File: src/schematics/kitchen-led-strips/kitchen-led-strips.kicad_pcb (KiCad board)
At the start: 4 copper layers, 55.5 x 80 mm, 73 parts, among them Q1 BC847BS, Q2 BC847BS, U1 DML3006LFDS, U2 AP62150WU, U3 PIC16F15355-I/MV

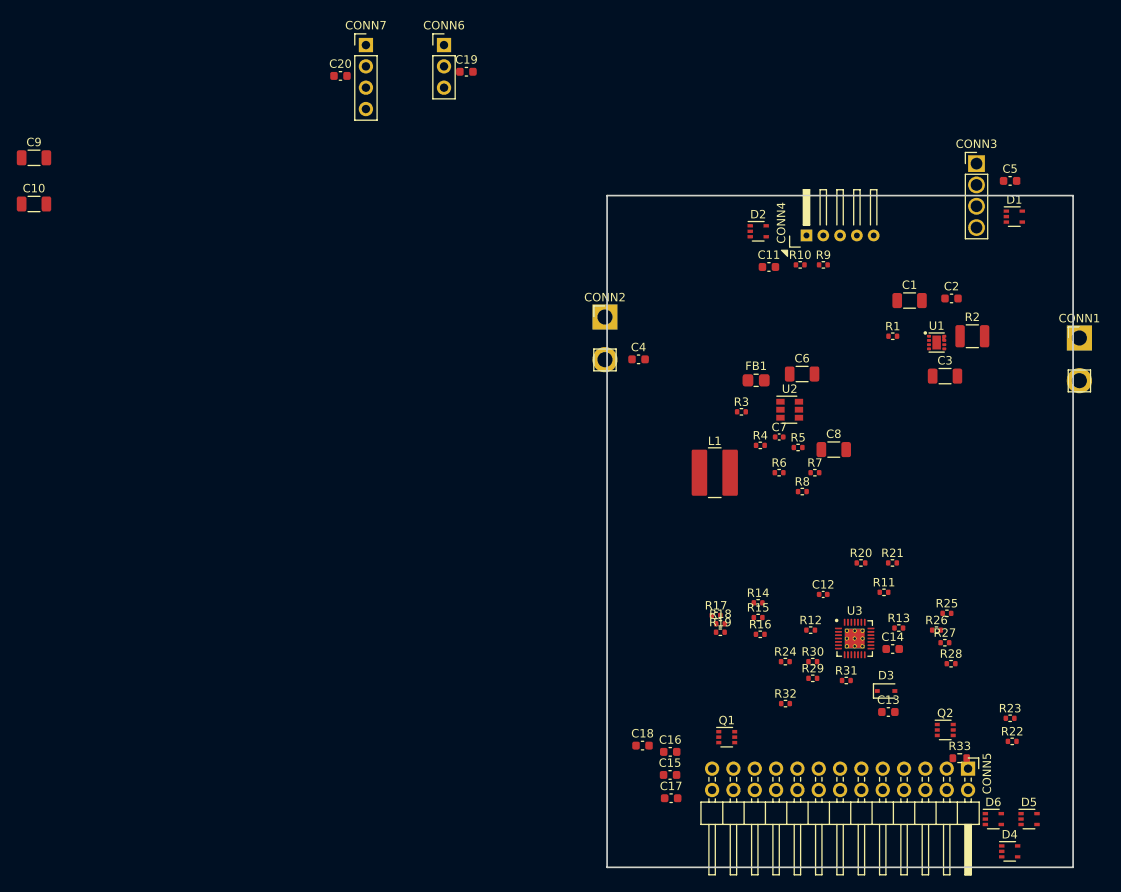
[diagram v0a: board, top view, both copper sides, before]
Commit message: Started the PCB layout.
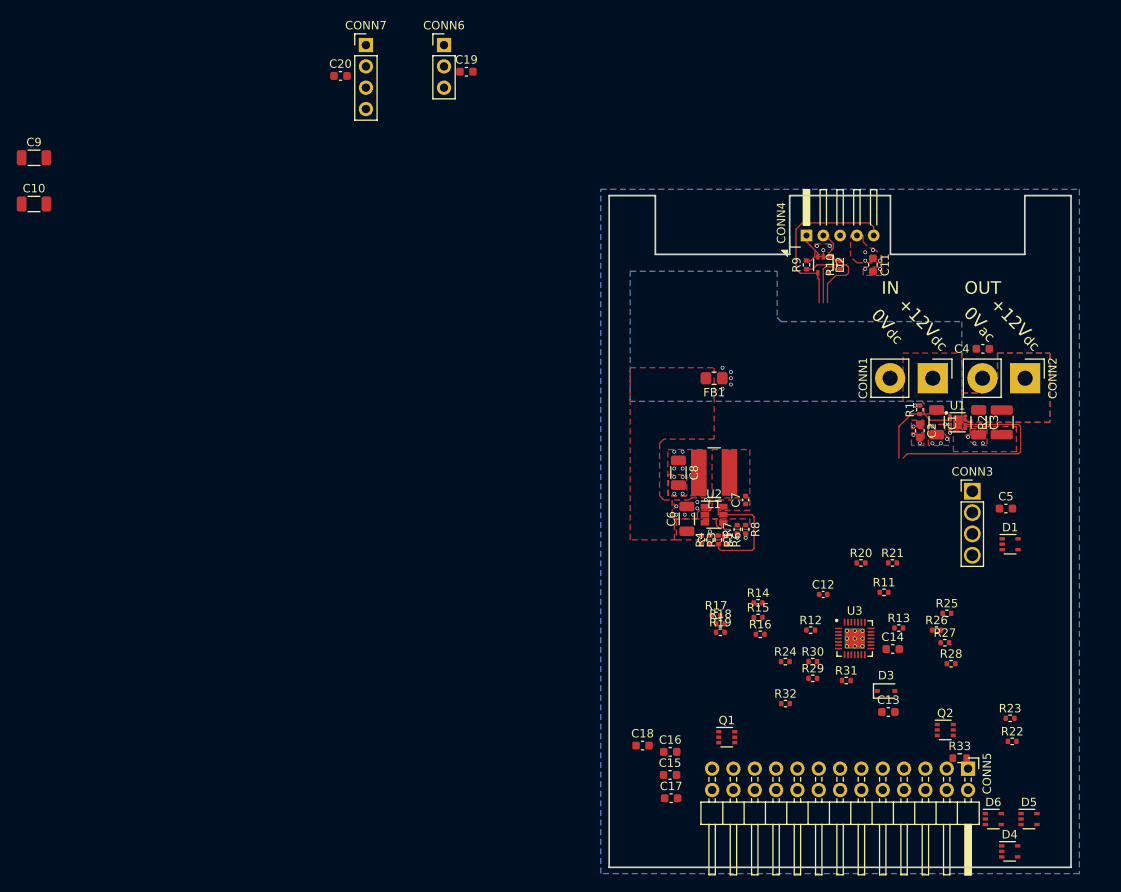
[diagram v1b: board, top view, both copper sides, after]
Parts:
- CONN1, CONN2: footprint restall-generic-connectors:th-header-1x2-5.08mm-vertical -> kitchen-led-strips:th-pads-1x2-5.08mm-vertical-2.5mm^2-solder-pads
- moved CONN2 47.7 mm to (219.5, 121.8), turned to -90 degrees
- moved C4 41.0 mm to (217.0, 118.2)
- moved C5 39.0 mm to (219.8, 137.3)
- moved CONN3 39.0 mm to (215.8, 139.0)
- moved D1 39.0 mm to (220.2, 141.5)
- moved C6 22.0 mm to (181.8, 138.5), turned to 90 degrees
- moved CONN1 20.1 mm to (208.5, 121.8), turned to -90 degrees
- moved C8 18.7 mm to (180.8, 133.0), turned to -90 degrees
- moved C2 16.2 mm to (209.5, 128.0), turned to -90 degrees
- moved R3 16.0 mm to (183.5, 141.0), turned to -90 degrees
- moved U2 15.4 mm to (185.0, 138.0)
- moved C1 14.9 mm to (211.5, 127.0), turned to -90 degrees
- moved R5 14.5 mm to (185.5, 141.0), turned to -90 degrees
- moved R4 12.8 mm to (184.5, 141.0), turned to 90 degrees
- moved C11 12.4 mm to (203.9, 108.2), turned to -90 degrees
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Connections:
- D2 pad 1: /MCU_ICSP_{CLK} -> /MCU_ICSP_{DAT}
- D2 pad 3: /MCU_ICSP_{DAT} -> /MCU_ICSP_{CLK}
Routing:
- net /VLED_{PG}: track 0.00 -> 24.0 mm
- net /~{MCU_MCLR}: track 0.00 -> 22.0 mm
- net Net-(R5-Pad2): track 0.00 -> 13.9 mm
- net Net-(R9-Pad1): track 0.00 -> 11.3 mm
- net /VLED_{EN}: track 0.00 -> 10.8 mm
- net Net-(R10-Pad1): track 0.00 -> 6.21 mm
- net /MCU_ICSP_{DAT}: track 0.00 -> 4.97 mm
- net /MCU_ICSP_{CLK}: track 0.00 -> 4.64 mm
- net GND: track 0.00 -> 3.39 mm, vias 0 -> 30
- net +5Vdc: track 0.00 -> 1.15 mm, vias 0 -> 15
- net /VLED: track 0.00 -> 1.03 mm
- net +12V_{dc}: vias 0 -> 1
- added copper zone on B.Cu, net +12V_{dc}
- added copper zone on F.Cu, net +12V_{dc}
- added copper zone on B.Cu, net +5Vdc
- added copper zone on F.Cu, net +5Vdc
- added copper zone on B.Cu, net /VLED
- added copper zone on F.Cu, net /VLED
- added copper zone on F.Cu, net GND
- added copper zone on In1.Cu, net GND
- added copper zone on In2.Cu, net GND
- added copper zone on F.Cu, net Net-(C1-Pad1)
- added copper zone on F.Cu, net Net-(C7-Pad1)
- added copper zone on F.Cu, net Net-(C7-Pad2)
- added copper zone on F.Cu, net Net-(R2-Pad1)
- added copper zone on F.Cu, net Net-(R7-Pad2)
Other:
- board size 55.5 x 80 mm -> 55 x 80 mm
- board text added: "+12V_{dc}"
- board text added: "0V_{ac}"
- board text added: "0V_{dc}"
- board text added: "IN"
- board text added: "OUT"
- board text added: "TODO: MIGHT BE NECESSARY TO MOVE +12V_{dc} ZONE FROM BOTTOM CU TO TOP CU SOONER, SO THAT +5V_{dc} CAN RUN ON BOTTOM CU UP THE LEFT-HAND-SIDE TO GET TO ICSP HEADER"
- board text added: "TODO: PLACE CONN3 NICELY"
- board text added: "TODO: PLACE SMPS NICELY"
- board text removed: "TODO: SHAPE / CUT BOARD OUTLINE FOR CONNECTOR NUTS"
- board text removed: "TODO: VIA PADS ONLY ON LAYERS THAT CONNECT; FOR THROUGH-HOLE PINS IT'S TOP, BOTTOM AND LAYERS THAT CONNECT"

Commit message: Further elaboration of the PCB.
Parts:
- moved C5 38.4 mm to (186.0, 119.0), turned to 180 degrees
- moved D1 37.9 mm to (186.0, 125.2), turned to -90 degrees
- moved D5 34.8 mm to (184.8, 164.8), turned to 90 degrees
- moved CONN3 34.4 mm to (186.0, 121.8), turned to -90 degrees
- moved C17 28.6 mm to (207.8, 165.5), turned to 180 degrees
- moved R33 26.2 mm to (188.5, 162.0)
- moved Q1 25.0 mm to (211.5, 164.8)
- moved D4 24.4 mm to (200.0, 164.8), turned to 90 degrees
- moved Q2 24.1 mm to (188.5, 164.8)
- moved C16 24.0 mm to (203.8, 165.5)
- moved R28 16.2 mm to (197.2, 158.8), turned to 90 degrees
- moved R25 16.0 mm to (200.2, 159.8), turned to 90 degrees
- moved R27 15.3 mm to (198.2, 158.8), turned to 90 degrees
- moved D6 14.2 mm to (215.2, 164.8), turned to 90 degrees
- moved R26 14.1 mm to (199.2, 158.8), turned to 90 degrees
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- renumbered D5 to D4, D6 to D5, D4 to D6
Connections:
- CONN5 pad 1: /IR_REC -> /I^{2}C_SDA
- CONN5 pad 13: /GPOC_{1} -> /GPIO_{3}
- CONN5 pad 15: /GPOC_{0} -> /GPIO_{2}
- CONN5 pad 17: +5Vdc -> /GPIO_{1}
- CONN5 pad 19: /GPIO_{3} -> /GPIO_{0}
- CONN5 pad 2: +5Vdc -> GND
- CONN5 pad 21: /GPIO_{2} -> +5Vdc
- CONN5 pad 23: /GPIO_{1} -> /IR_LED
- CONN5 pad 25: /GPIO_{0} -> /IR_REC
- CONN5 pad 26: GND -> +5Vdc
- CONN5 pad 3: /IR_LED -> /I^{2}C_SCL
- CONN5 pad 7: /I^{2}C_SDA -> /GPOC_{1}
- CONN5 pad 9: /I^{2}C_SCL -> /GPOC_{0}
- D1 pad 1: /LED_{D1} -> +5Vdc
- D1 pad 3: /LED_{D0} -> +5Vdc
- D1 pad 4: +5Vdc -> /LED_{D1}
- D1 pad 5: +5Vdc -> /LED_{D0}
- D4 pad 4: /GPIO_{2} -> /GPIO_{3}
- D4 pad 5: /GPIO_{3} -> /GPIO_{2}
- D5 pad 1: /GPOC_{1} -> /IR_LED
- D5 pad 3: /GPOC_{0} -> /IR_REC
- D6 pad 1: /IR_LED -> /GPOC_{1}
- D6 pad 3: /IR_REC -> /I^{2}C_SCL
- D6 pad 4: /I^{2}C_SCL -> /I^{2}C_SDA
- D6 pad 5: /I^{2}C_SDA -> /GPOC_{0}
- Q1 pad 3: /GPOC_{1} -> /GPOC_{0}
- Q1 pad 6: /GPOC_{0} -> /GPOC_{1}
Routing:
- net Net-(R9-Pad1): track 11.3 -> 53.8 mm
- net Net-(R10-Pad1): track 6.21 -> 48.0 mm
- net /~{MCU_MCLR}: track 22.0 -> 63.2 mm
- net /LED_{D1}: track 0.00 -> 40.0 mm
- net /LED_{D0}: track 0.00 -> 39.3 mm
- net /VLED_{PG}: track 24.0 -> 58.8 mm
- net /VLED_{EN}: track 10.8 -> 37.7 mm
- net /I^{2}C_SDA: track 0.00 -> 23.5 mm
- net /I^{2}C_SCL: track 0.00 -> 22.7 mm
- net /GPOC_{0}: track 0.00 -> 18.2 mm
- net /GPOC_{1}: track 0.00 -> 14.1 mm
- net Net-(Q1-Pad5): track 0.00 -> 12.9 mm
- net Net-(Q1-Pad2): track 0.00 -> 11.7 mm
- net /VIN_{MON}: track 0.00 -> 7.67 mm
- net /DEBUG_{0}: track 0.00 -> 7.31 mm
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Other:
- board text added: "TODO: PLACE SMPS NICELY - MAYBE OVER THE RHS OF THE BOARD ?"
- board text added: "TODO: THIS CONNECTOR IS 'IN' (LHS WHEN LOOKING AT CASE)"
- board text added: "TODO: THIS CONNECTOR IS 'OUT' (RHS WHEN LOOKING AT CASE)"
- board text removed: "TODO: MIGHT BE NECESSARY TO MOVE +12V_{dc} ZONE FROM BOTTOM CU TO TOP CU SOONER, SO THAT +5V_{dc} CAN RUN ON BOTTOM CU UP THE LEFT-HAND-SIDE TO GET TO ICSP HEADER"
- board text removed: "TODO: PLACE CONN3 NICELY"
- board text removed: "TODO: PLACE SMPS NICELY"

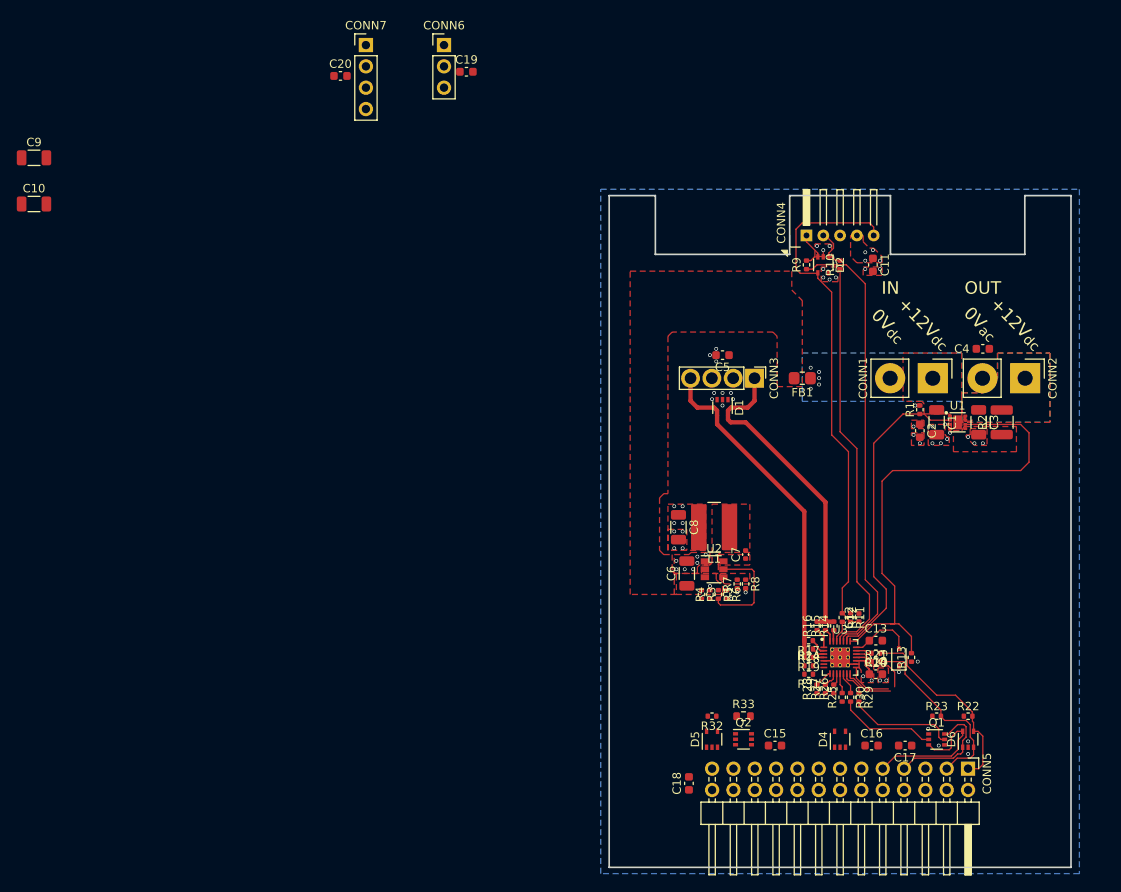
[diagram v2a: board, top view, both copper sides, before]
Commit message: Further PCB elaboration.  Almost ready for fabrication.
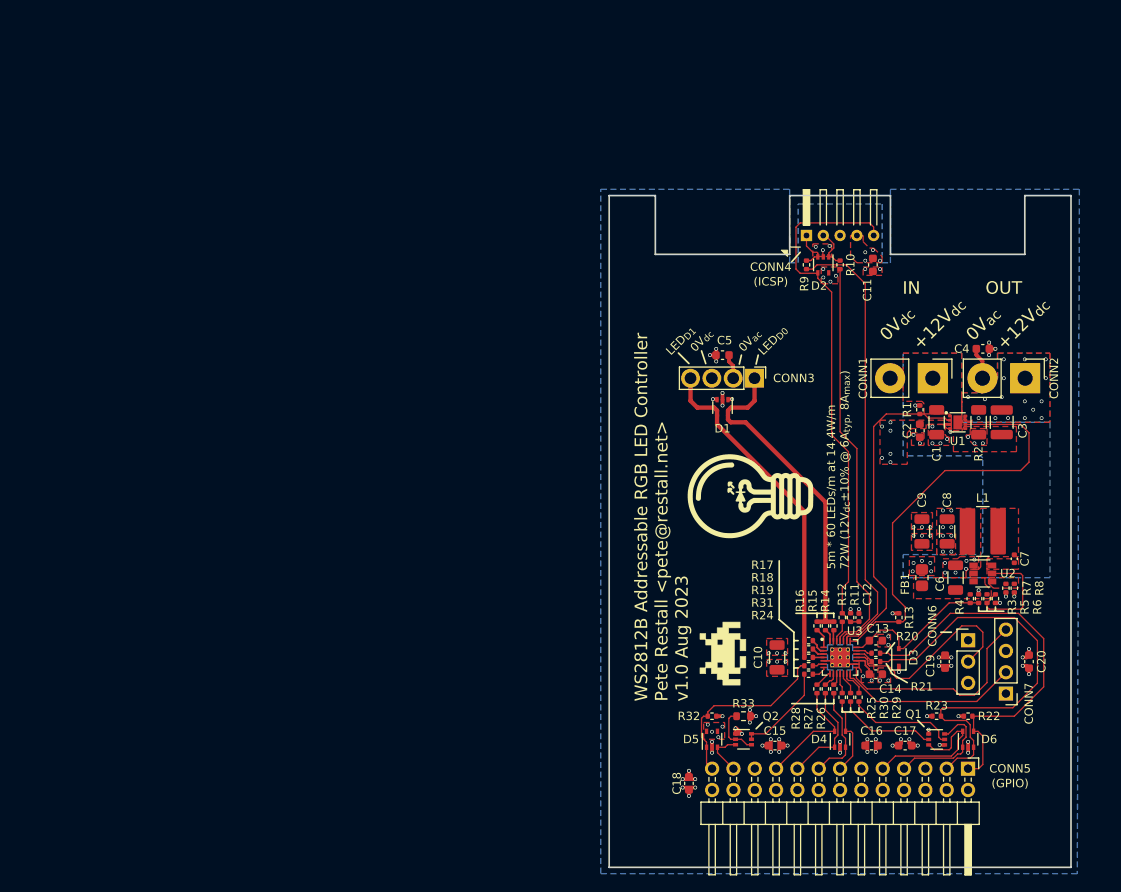
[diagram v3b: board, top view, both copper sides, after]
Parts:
- moved C9 114.7 mm to (209.8, 140.0), turned to -90 degrees
- moved C20 107.7 mm to (222.5, 155.5), turned to 90 degrees
- moved C10 103.7 mm to (192.5, 155.0), turned to -90 degrees
- moved CONN7 103.2 mm to (219.8, 155.5), turned to 180 degrees
- moved CONN6 94.5 mm to (215.2, 155.5)
- moved C19 90.5 mm to (212.5, 155.5), turned to -90 degrees
- moved C6 32.0 mm to (213.8, 145.5)
- moved C7 32.0 mm to (220.8, 143.2)
- moved C8 32.0 mm to (212.8, 140.0)
- moved L1 32.0 mm to (217.0, 140.0)
- moved R3 32.0 mm to (215.5, 148.0)
- moved R4 32.0 mm to (216.5, 148.0)
- moved R5 32.0 mm to (217.5, 148.0)
- moved R6 32.0 mm to (218.5, 148.0)
- moved R7 32.0 mm to (219.8, 146.8)
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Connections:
- D4 pad 1: /GPIO_{0} -> /GPIO_{1}
- D4 pad 3: /GPIO_{1} -> /GPIO_{2}
- D4 pad 5: /GPIO_{2} -> /GPIO_{0}
- D5 pad 1: /IR_LED -> /IR_REC
- D5 pad 3: /IR_REC -> /IR_LED
- Q2 pad 1: Net-(Q2-Pad1) -> GND
- Q2 pad 3: Net-(Q2-Pad2) -> /IR_LED
- Q2 pad 4: GND -> Net-(Q2-Pad2)
- Q2 pad 5: Net-(Q2-Pad1) -> Net-(Q2-Pad5)
- Q2 pad 6: /IR_LED -> Net-(Q2-Pad5)
- R24 pad 1: Net-(Q2-Pad2) -> Net-(Q2-Pad5)
- R24 pad 2: Net-(R24-Pad2) -> Net-(U3-Pad7)
- R33 pad 1: Net-(Q2-Pad1) -> Net-(Q2-Pad2)
- U3 pad 6: Net-(R24-Pad2) -> Net-(R31-Pad1)
- U3 pad 7: Net-(R31-Pad1) -> Net-(U3-Pad7)
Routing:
- net /I^{2}C_SCL: track 22.7 -> 52.3 mm
- net GND: track 6.61 -> 33.3 mm, vias 41 -> 75
- net /I^{2}C_SDA: track 23.5 -> 47.1 mm
- net /IR_REC: track 0.00 -> 22.3 mm
- net /DEBUG_{2}: track 5.61 -> 25.5 mm
- net /DEBUG_{0}: track 7.31 -> 23.8 mm
- net /DEBUG_{1}: track 5.94 -> 21.7 mm
- net +5Vdc: track 3.96 -> 19.6 mm, vias 27 -> 53
- net /GPIO_{0}: track 0.00 -> 14.2 mm
- net /GPIO_{1}: track 0.00 -> 12.7 mm
- net /GPIO_{2}: track 0.00 -> 11.8 mm
- net /VIN_{MON}: track 7.67 -> 19.4 mm
- net Net-(Q2-Pad5): track 0.00 -> 11.4 mm
- net /GPIO_{3}: track 0.00 -> 9.51 mm
- net /VLED_{PG}: track 58.8 -> 50.5 mm
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- added copper zone on B.Cu, net GND
- added copper zone on B.Cu, net Net-(C1-Pad1)
- removed copper zone on B.Cu, net +12V_{dc}
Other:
- board text added: "(GPIO)"
- board text added: "(ICSP)"
- board text added: "5m * 60 LEDs/m at 14.4W/m 72W (12V_{dc}±10% @ 6A_{typ}, 8A_{max})"
- board text added: "Fabrication by JLCPCB. Stackup: JLC04161H-7628 L1 - Signal / Power L2 - GND L3 - GND L4 - Signal / Power"
- board text added: "JLCJLCJLCJLC"
- board text added: "LED_{D0}"
- board text added: "LED_{D1}"
- board text added: "TODO: GROUND STITCHING"
- board text added: "TODO: SILKSCREEN / FAB ORGANISATION"
- board text added: "WS2812B Addressable RGB LED Controller Pete Restall <pete@restall.net> v1.0 Aug 2023"
- board text removed: "TODO: PLACE SMPS NICELY - MAYBE OVER THE RHS OF THE BOARD ?"

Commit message: Final PCB tweaks.  Generated the gerbers for fabrication.
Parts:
- turned CONN6 to 180 degrees
- turned R13 to 90 degrees
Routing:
- net +5Vdc: track 19.6 -> 22.8 mm
- net /VLED_{PG}: track 50.5 -> 48.8 mm
- net GND: track 33.3 -> 33.2 mm, vias 75 -> 394
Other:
- board text added: "+5V"
- board text added: "0V"
- board text added: "5m * 60 LEDs/m at 14.4W/m 72W_{typ} (12V_{dc}±10% @ 6A_{typ}, 8A_{max})"
- board text added: "DB_{0}"
- board text added: "DB_{1}"
- board text added: "DB_{2}"
- board text removed: "5m * 60 LEDs/m at 14.4W/m 72W (12V_{dc}±10% @ 6A_{typ}, 8A_{max})"
- board text removed: "TODO: GROUND STITCHING"
- board text removed: "TODO: SILKSCREEN / FAB ORGANISATION"
- board text removed: "TODO: THIS CONNECTOR IS 'IN' (LHS WHEN LOOKING AT CASE)"
- board text removed: "TODO: THIS CONNECTOR IS 'OUT' (RHS WHEN LOOKING AT CASE)"
